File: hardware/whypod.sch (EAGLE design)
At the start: 100 parts, among them IC1 IC_USBLC6-2, J1 AUDIO_JACK_TRRSSMD_RA, U1 USD-SOCKETUSD, X2 USB-A-S, Y2 CRYSTAL-GROUNDEDSMD-5X3.2

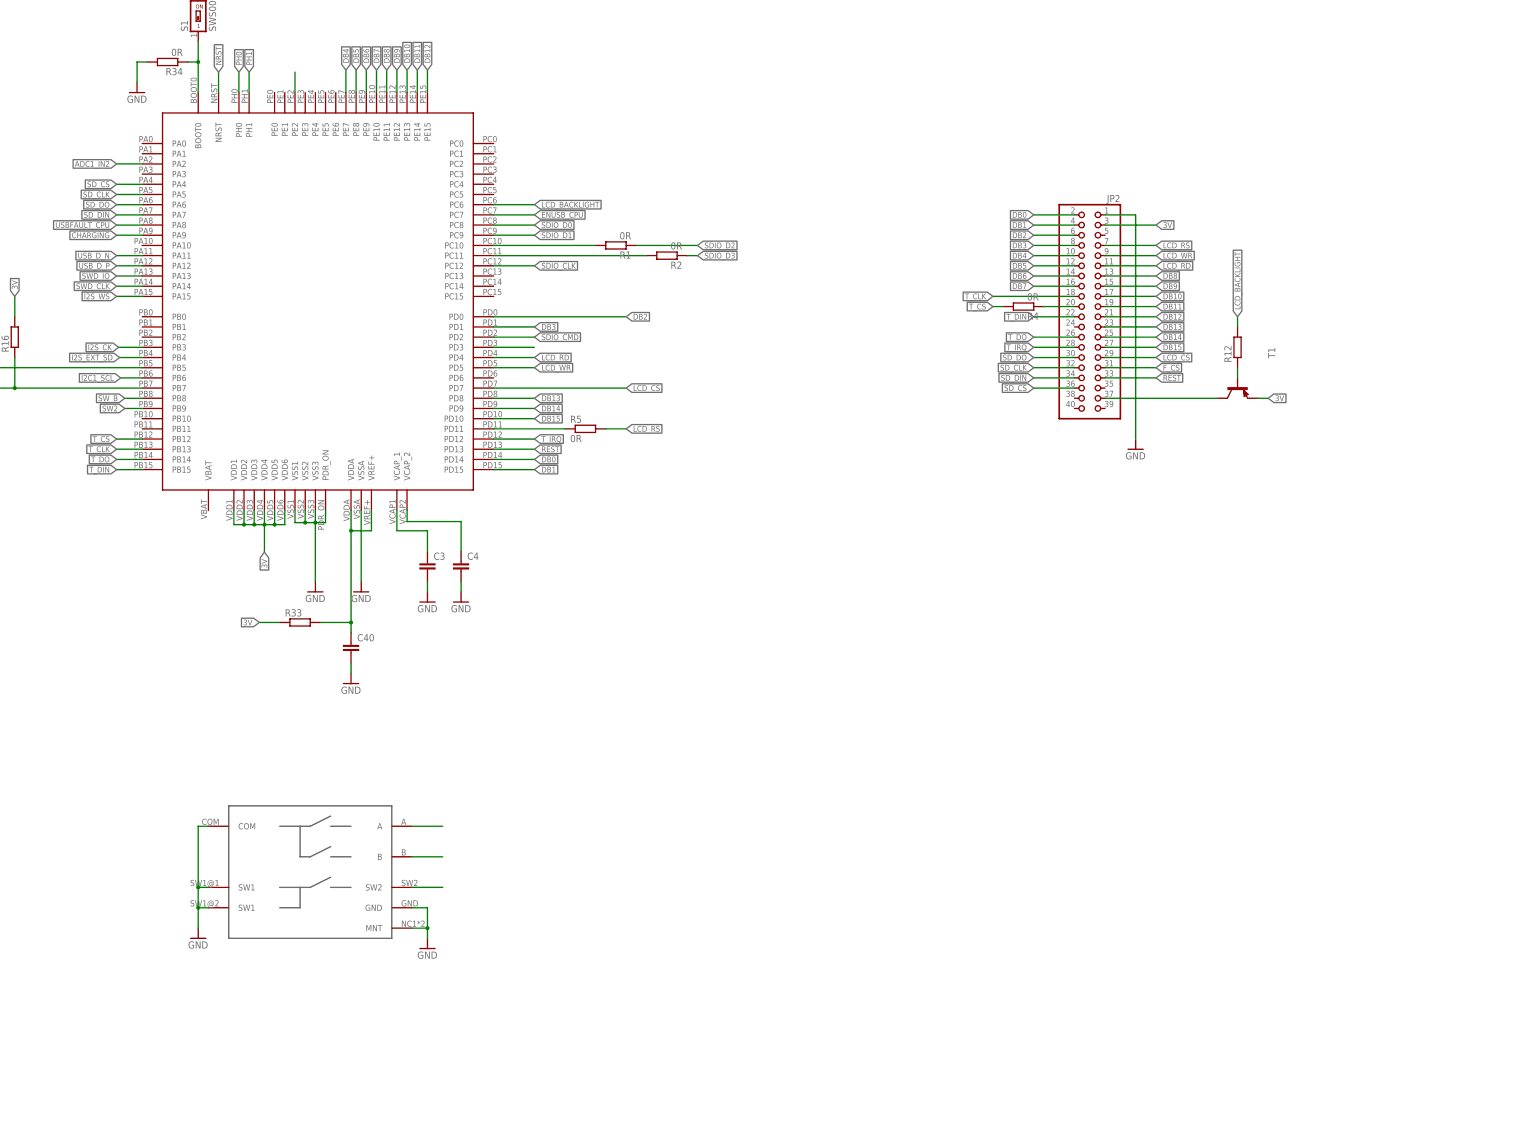
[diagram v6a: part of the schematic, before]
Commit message: Switches added
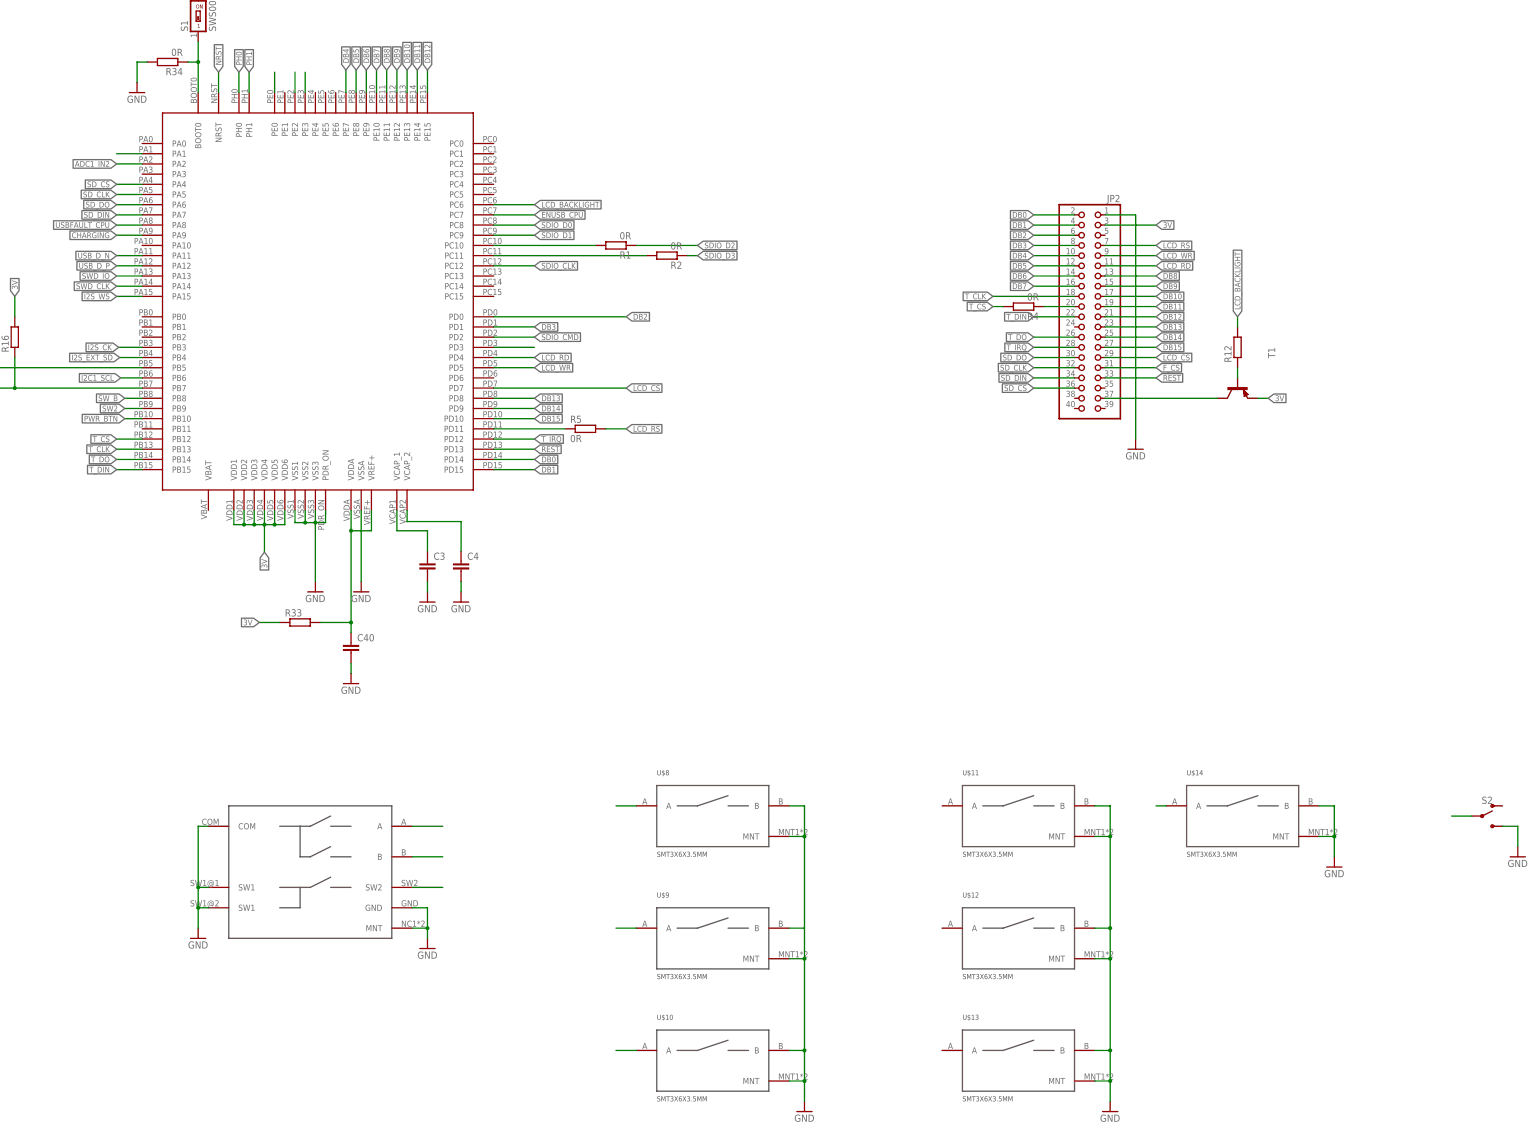
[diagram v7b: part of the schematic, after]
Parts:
- added S2: (no value), SparkFun-Switches:SWITCH-SPDT-SMD-RIGHT-ANGLE
- added U$10, U$11, U$12, U$13, U$14, U$8, U$9: SMT3X6X3.5MM, mw:SMT3X6X3.5MM
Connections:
- new net LOCK_SWITCH: S2.P, U$2.PA1
- new net PWR_BTN: U$2.PB10, U$8.A
- new net VOL_DN: U$10.A, U$2.PE3
- new net VOL_UP: U$2.PE0, U$9.A
- net GND: now also S2.S, U$10.B, U$10.MNT, U$11.B, U$11.MNT, U$12.B, U$12.MNT, U$13.B, U$13.MNT, U$14.B, U$14.MNT, U$8.B, U$8.MNT, U$9.B, U$9.MNT
- net NRST: now also U$14.A
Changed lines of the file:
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@@
 <part name="GND56" library="supply1" deviceset="GND" device=""/>
 <part name="R35" library="rcl" deviceset="R-EU_" device="R0603"/>
+<part name="U$8" library="mw" deviceset="SMT3X6X3.5MM" device=""/>
+<part name="U$9" library="mw" deviceset="SMT3X6X3.5MM" device=""/>
+<part name="U$10" library="mw" deviceset="SMT3X6X3.5MM" device=""/>
+<part name="GND35" library="supply1" deviceset="GND" device=""/>
+<part name="U$11" library="mw" deviceset="SMT3X6X3.5MM" device=""/>
+<part name="U$12" library="mw" deviceset="SMT3X6X3.5MM" device=""/>
+<part name="U$13" library="mw" deviceset="SMT3X6X3.5MM" device=""/>
+<part name="GND4" library="supply1" deviceset="GND" device=""/>
+<part name="U$14" library="mw" deviceset="SMT3X6X3.5MM" device=""/>
+<part name="GND5" library="supply1" deviceset="GND" device=""/>
+<part name="S2" library="SparkFun-Switches" deviceset="SWITCH-SPDT" device="-SMD-RIGHT-ANGLE"/>
+<part name="GND57" library="supply1" deviceset="GND" device=""/>
 </parts>
 <sheets>
@@
 <instance part="GND56" gate="1" x="116.84" y="114.3"/>
 <instance part="R35" gate="G$1" x="398.78" y="220.98" rot="R90"/>
+<instance part="U$8" gate="G$1" x="299.72" y="-99.06"/>
+<instance part="U$9" gate="G$1" x="299.72" y="-129.54"/>
+<instance part="U$10" gate="G$1" x="299.72" y="-160.02"/>
+<instance part="GND35" gate="1" x="323.85" y="-177.8"/>
+<instance part="U$11" gate="G$1" x="375.92" y="-99.06"/>
+<instance part="U$12" gate="G$1" x="375.92" y="-129.54"/>
+<instance part="U$13" gate="G$1" x="375.92" y="-160.02"/>
+<instance part="GND4" gate="1" x="400.05" y="-177.8"/>
+<instance part="U$14" gate="G$1" x="431.8" y="-99.06"/>
+<instance part="GND5" gate="1" x="455.93" y="-116.84"/>
+<instance part="S2" gate="1" x="492.76" y="-104.14"/>
+<instance part="GND57" gate="1" x="501.65" y="-114.3"/>
 </instances>
 <busses>
@@
 <wire x1="119.38" y1="121.92" x2="116.84" y2="121.92" width="0.1524" layer="91"/>
 <wire x1="116.84" y1="121.92" x2="116.84" y2="116.84" width="0.1524" layer="91"/>
+</segment>
+<segment>
+<pinref part="U$10" gate="G$1" pin="MNT"/>
+<pinref part="GND35" gate="1" pin="GND"/>
+<wire x1="320.04" y1="-170.18" x2="323.85" y2="-170.18" width="0.1524" layer="91"/>
+<wire x1="323.85" y1="-170.18" x2="323.85" y2="-175.26" width="0.1524" layer="91"/>
+<pinref part="U$10" gate="G$1" pin="B"/>
+<wire x1="320.04" y1="-162.56" x2="323.85" y2="-162.56" width="0.1524" layer="91"/>
+<wire x1="323.85" y1="-162.56" x2="323.85" y2="-170.18" width="0.1524" layer="91"/>
+<junction x="323.85" y="-170.18"/>
+<pinref part="U$8" gate="G$1" pin="MNT"/>
+<wire x1="320.04" y1="-109.22" x2="323.85" y2="-109.22" width="0.1524" layer="91"/>
+<pinref part="U$8" gate="G$1" pin="B"/>
+<wire x1="320.04" y1="-101.6" x2="323.85" y2="-101.6" width="0.1524" layer="91"/>
+<wire x1="323.85" y1="-101.6" x2="323.85" y2="-109.22" width="0.1524" layer="91"/>
+<junction x="323.85" y="-109.22"/>
+<pinref part="U$9" gate="G$1" pin="MNT"/>
+<wire x1="320.04" y1="-139.7" x2="323.85" y2="-139.7" width="0.1524" layer="91"/>
+<pinref part="U$9" gate="G$1" pin="B"/>
+<wire x1="320.04" y1="-132.08" x2="323.85" y2="-132.08" width="0.1524" layer="91"/>
+<junction x="323.85" y="-139.7"/>
+<wire x1="323.85" y1="-132.08" x2="323.85" y2="-139.7" width="0.1524" layer="91"/>
+<wire x1="323.85" y1="-109.22" x2="323.85" y2="-132.08" width="0.1524" layer="91"/>
+<wire x1="323.85" y1="-139.7" x2="323.85" y2="-162.56" width="0.1524" layer="91"/>
+<junction x="323.85" y="-162.56"/>
+</segment>
+<segment>
+<pinref part="GND4" gate="1" pin="GND"/>
+<wire x1="400.05" y1="-175.26" x2="400.05" y2="-170.18" width="0.1524" layer="91"/>
+<pinref part="U$13" gate="G$1" pin="MNT"/>
+<wire x1="396.24" y1="-170.18" x2="400.05" y2="-170.18" width="0.1524" layer="91"/>
+<pinref part="U$13" gate="G$1" pin="B"/>
+<wire x1="396.24" y1="-162.56" x2="400.05" y2="-162.56" width="0.1524" layer="91"/>
+<wire x1="400.05" y1="-162.56" x2="400.05" y2="-170.18" width="0.1524" layer="91"/>
+<junction x="400.05" y="-170.18"/>
+<pinref part="U$12" gate="G$1" pin="MNT"/>
+<wire x1="396.24" y1="-139.7" x2="400.05" y2="-139.7" width="0.1524" layer="91"/>
+<wire x1="400.05" y1="-139.7" x2="400.05" y2="-162.56" width="0.1524" layer="91"/>
+<junction x="400.05" y="-162.56"/>
+<pinref part="U$12" gate="G$1" pin="B"/>
+<wire x1="396.24" y1="-132.08" x2="400.05" y2="-132.08" width="0.1524" layer="91"/>
+<wire x1="400.05" y1="-132.08" x2="400.05" y2="-139.7" width="0.1524" layer="91"/>
+<junction x="400.05" y="-139.7"/>
+<pinref part="U$11" gate="G$1" pin="MNT"/>
+<wire x1="396.24" y1="-109.22" x2="400.05" y2="-109.22" width="0.1524" layer="91"/>
+<wire x1="400.05" y1="-109.22" x2="400.05" y2="-132.08" width="0.1524" layer="91"/>
+<junction x="400.05" y="-132.08"/>
+<pinref part="U$11" gate="G$1" pin="B"/>
+<wire x1="396.24" y1="-101.6" x2="400.05" y2="-101.6" width="0.1524" layer="91"/>
+<wire x1="400.05" y1="-101.6" x2="400.05" y2="-109.22" width="0.1524" layer="91"/>
+<junction x="400.05" y="-109.22"/>
+</segment>
+<segment>
+<pinref part="U$14" gate="G$1" pin="B"/>
+<pinref part="GND5" gate="1" pin="GND"/>
+<wire x1="452.12" y1="-101.6" x2="455.93" y2="-101.6" width="0.1524" layer="91"/>
+<wire x1="455.93" y1="-101.6" x2="455.93" y2="-109.22" width="0.1524" layer="91"/>
+<wire x1="455.93" y1="-109.22" x2="455.93" y2="-114.3" width="0.1524" layer="91"/>
+<wire x1="452.12" y1="-109.22" x2="455.93" y2="-109.22" width="0.1524" layer="91"/>
+<junction x="455.93" y="-109.22"/>
+<pinref part="U$14" gate="G$1" pin="MNT"/>
+</segment>
+<segment>
+<pinref part="S2" gate="1" pin="S"/>
+<pinref part="GND57" gate="1" pin="GND"/>
+<wire x1="497.84" y1="-106.68" x2="501.65" y2="-106.68" width="0.1524" layer="91"/>
+<wire x1="501.65" y1="-106.68" x2="501.65" y2="-111.76" width="0.1524" layer="91"/>
 </segment>
 </net>
@@
 <junction x="398.78" y="203.2"/>
 </segment>
+<segment>
+<pinref part="U$14" gate="G$1" pin="A"/>
+<wire x1="414.02" y1="-101.6" x2="411.48" y2="-101.6" width="0.1524" layer="91"/>
+</segment>
 </net>
 <net name="AGND" class="0">
@@
 </segment>
 </net>
+<net name="VOL_UP" class="0">
+<segment>
+<pinref part="U$2" gate="G$1" pin="PE0"/>
+<wire x1="191.77" y1="76.2" x2="191.77" y2="81.28" width="0.1524" layer="91"/>
+</segment>
+<segment>
+<pinref part="U$9" gate="G$1" pin="A"/>
+<wire x1="281.94" y1="-132.08" x2="276.86" y2="-132.08" width="0.1524" layer="91"/>
+</segment>
+</net>
+<net name="VOL_DN" class="0">
+<segment>
+<pinref part="U$10" gate="G$1" pin="A"/>
+<wire x1="281.94" y1="-162.56" x2="276.86" y2="-162.56" width="0.1524" layer="91"/>
+</segment>
+<segment>
+<pinref part="U$2" gate="G$1" pin="PE3"/>
+<wire x1="199.39" y1="76.2" x2="199.39" y2="81.28" width="0.1524" layer="91"/>
+</segment>
+</net>
+<net name="PWR_BTN" class="0">
+<segment>
+<pinref part="U$2" gate="G$1" pin="PB10"/>
+<wire x1="158.75" y1="-5.08" x2="154.432" y2="-5.08" width="0.1524" layer="91"/>
+<label x="154.432" y="-5.08" size="1.4224" layer="95" rot="R180" xref="yes"/>
+</segment>
+<segment>
+<pinref part="U$8" gate="G$1" pin="A"/>
+<wire x1="281.94" y1="-101.6" x2="276.86" y2="-101.6" width="0.1524" layer="91"/>
+</segment>
+</net>
+<net name="LOCK_SWITCH" class="0">
+<segment>
+<pinref part="S2" gate="1" pin="P"/>
+<wire x1="490.22" y1="-104.14" x2="485.14" y2="-104.14" width="0.1524" layer="91"/>
+</segment>
+<segment>
+<pinref part="U$2" gate="G$1" pin="PA1"/>
+<wire x1="158.75" y1="60.96" x2="152.4" y2="60.96" width="0.1524" layer="91"/>
+</segment>
+</net>

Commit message: 32kHz oscillator added
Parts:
- added C1, C2, C46: (no value), rcl:C-EUC0603
- added C44, C45: (no value), rcl:C-EUC0402
- added X1: CRYSTALS-NOGND-CFPX-217, IQD-Frequency-Products:CRYSTALS-NOGND-CFPX-217
- C7: device rcl:C-EUC0603 -> rcl:C-EUC0402
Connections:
- new net KEY_1: U$11.A, U$2.PC2
- new net KEY_2: U$12.A, U$2.PC3
- new net KEY_3: U$13.A, U$2.PA0
- new net N$30: C44.1, U$2.VBAT
- new net OSC32_IN: C1.2, U$2.PC14, X1.1
- new net OSC32_OUT: C2.2, U$2.PC15, X1.2
- net 3V: now also C45.1
- net GND: now also C1.1, C2.1, C44.2, C45.2, C46.2
- net NRST: now also C46.1
- net SW_A: now also U$2.PE3; no longer U$2.PE2
- net VOL_DN: now also U$2.PE2; no longer U$2.PE3
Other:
- moved on the sheet: C10, C15, C16, C17, C18, C19, C20, C21, C22, C41, C43, C5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
